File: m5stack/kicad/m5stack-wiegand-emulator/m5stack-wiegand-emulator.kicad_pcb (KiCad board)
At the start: 2 copper layers, 50 x 50 mm, 58 parts, among them J1 2x15 socket header, J2 2x15 pin header, J3 1x5 female, M1 M5 Stack 3.1mm mounting hole, M12 M5 Stack 1.1mm reference hole, M2 M5 Stack 3.1mm mounting hole, M3 M5 Stack 3.1mm mounting hole, M4 M5 Stack 3.1mm mounting hole, M5 M5 Stack 2mm mounting hole, M6 M5 Stack 2mm mounting hole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

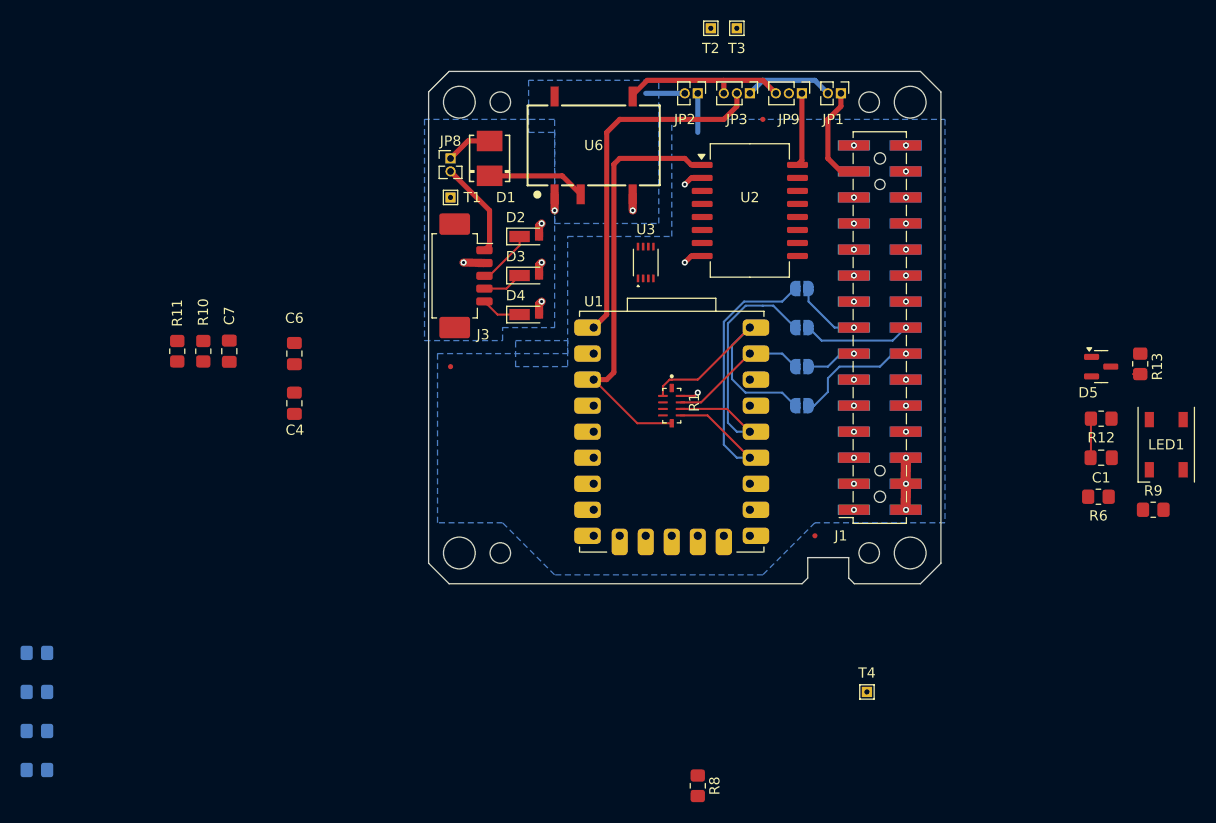
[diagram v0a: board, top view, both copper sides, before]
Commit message: M5: routed DI/DO signals
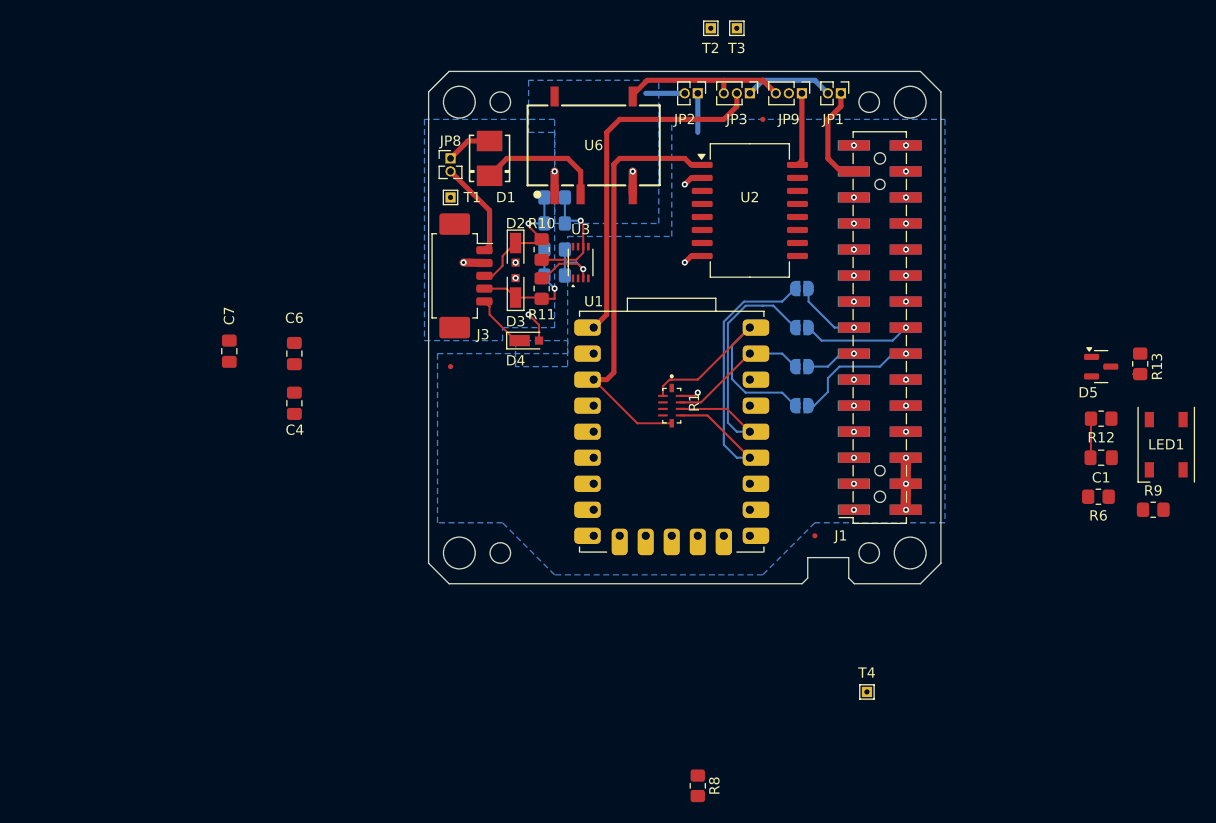
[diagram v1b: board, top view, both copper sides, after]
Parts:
- moved R19 69.9 mm to (101.6, 83.8)
- moved R15 69.9 mm to (101.6, 76.2)
- moved R16 69.0 mm to (101.6, 81.3)
- moved R14 65.6 mm to (101.6, 78.7)
- moved R11 36.1 mm to (100.3, 85.1)
- moved R10 34.5 mm to (100.3, 81.3)
- moved U3 6.35 mm to (104.1, 82.5)
- moved D4 2.54 mm to (99.1, 90.2)
- moved D2 1.98 mm to (97.8, 81.5), turned to -90 degrees
- moved D3 1.80 mm to (97.8, 85.1), turned to 90 degrees
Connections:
- R10 pad 1: Net-(U3-1Y) -> /DI
- R10 pad 2: /DI -> Net-(U3-1Y)
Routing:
- net Net-(U3-1Y): track 0.00 -> 11.8 mm, vias 0 -> 1
- net Net-(U3-2Y): track 0.00 -> 10.4 mm, vias 0 -> 1
- net /DO: track 4.35 -> 12.5 mm, vias 0 -> 1
- net /DI: track 5.93 -> 13.8 mm, vias 0 -> 1
- net Net-(D1-K): track 9.64 -> 12.4 mm
- net /LED: track 3.96 -> 5.47 mm

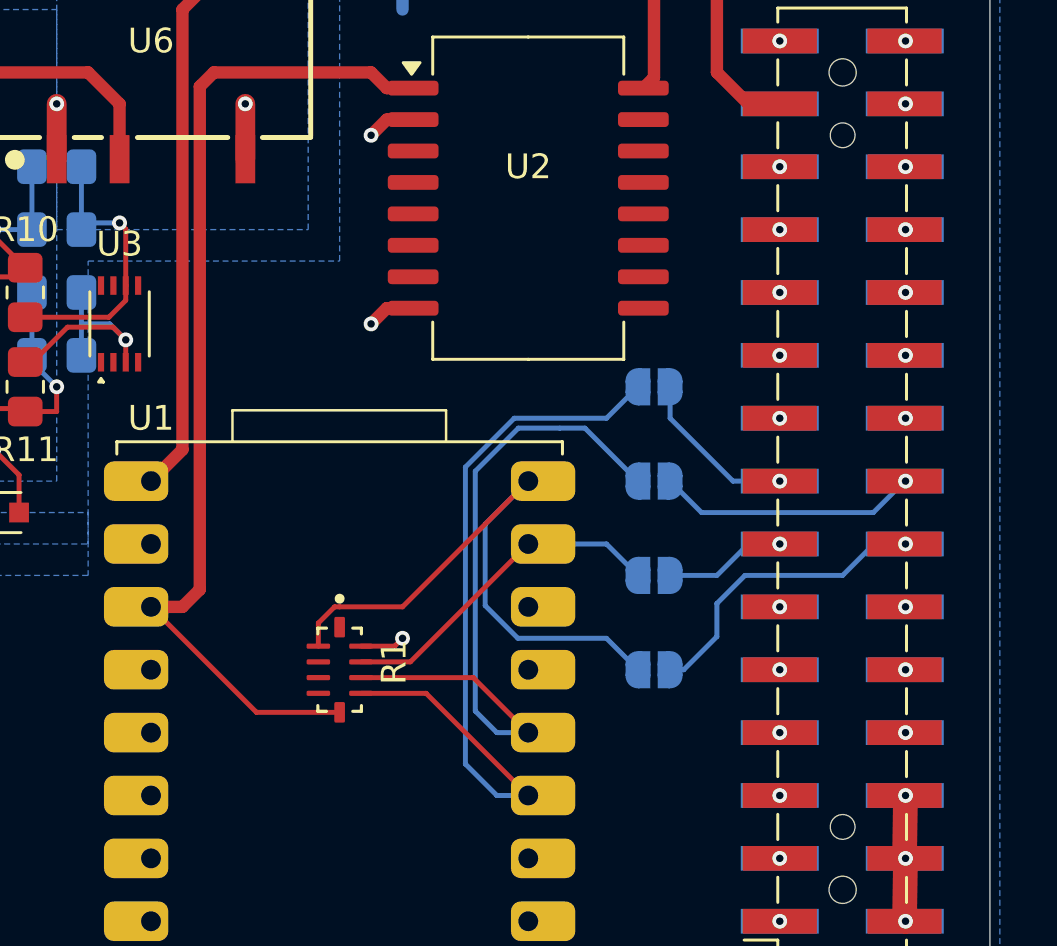
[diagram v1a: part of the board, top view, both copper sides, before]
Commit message: M5: moved DI/DO to GP28/29"
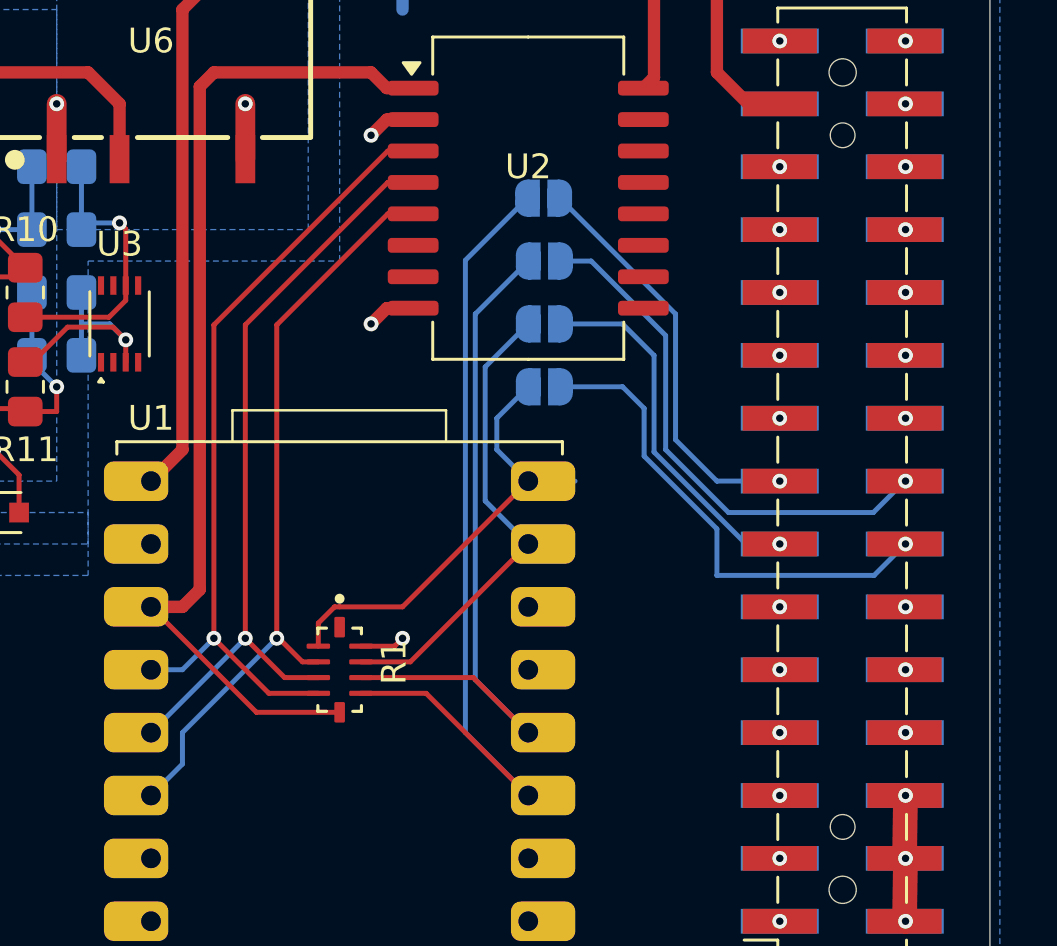
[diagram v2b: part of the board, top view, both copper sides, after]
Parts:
- moved JP4 12.3 mm to (121.3, 85.1)
- moved JP5 11.1 mm to (121.3, 82.5)
- moved JP6 9.93 mm to (121.3, 80.0)
- moved JP7 8.83 mm to (121.3, 77.5)
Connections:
- U1 pad 10: Net-(R1B-R2.2) -> unconnected-(U1-GP13-Pad10)
- U1 pad 4: unconnected-(U1-GP29-Pad4) -> Net-(R1D-R4.2)
- U1 pad 5: unconnected-(U1-GP28-Pad5) -> Net-(R1C-R3.2)
- U1 pad 6: unconnected-(U1-GP27-Pad6) -> Net-(R1B-R2.2)
- U1 pad 8: Net-(R1D-R4.2) -> unconnected-(U1-GP15-Pad8)
- U1 pad 9: Net-(R1C-R3.2) -> unconnected-(U1-GP14-Pad9)
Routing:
- net Net-(R1D-R4.2): track 0.00 -> 31.8 mm, vias 0 -> 1
- net Net-(R1C-R3.2): track 0.00 -> 30.8 mm, vias 0 -> 1
- net Net-(R1B-R2.2): track 0.00 -> 30.6 mm, vias 0 -> 1
- net /TXD1: track 4.96 -> 16.1 mm
- net /RXD2: track 10.5 -> 21.3 mm
- net /TXD2: track 6.75 -> 16.6 mm
- net /RXD1: track 12.4 -> 19.9 mm
- net Net-(JP4-B): track 24.8 -> 18.5 mm
- net Net-(JP5-B): track 13.7 -> 19.1 mm
- net Net-(JP7-B): track 31.8 -> 34.7 mm

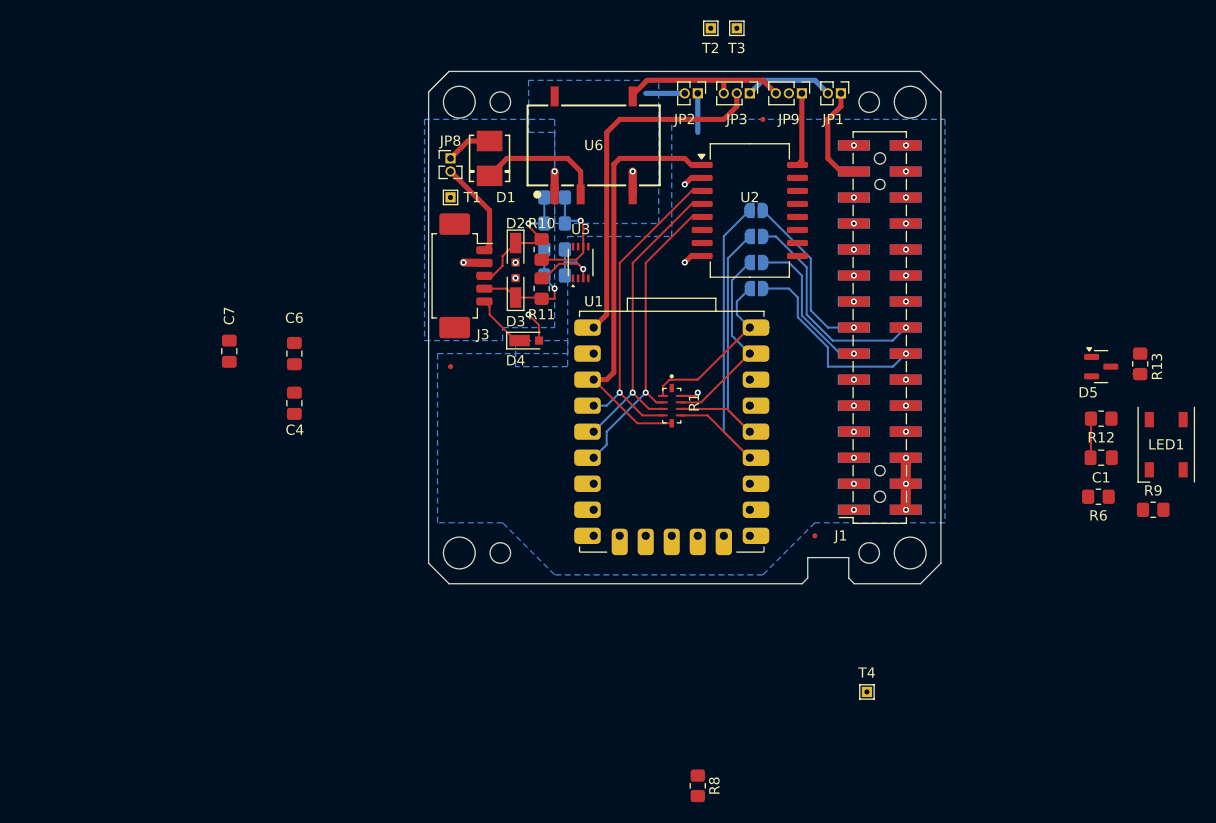
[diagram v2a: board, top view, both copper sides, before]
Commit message: M5: routing LED IN signal
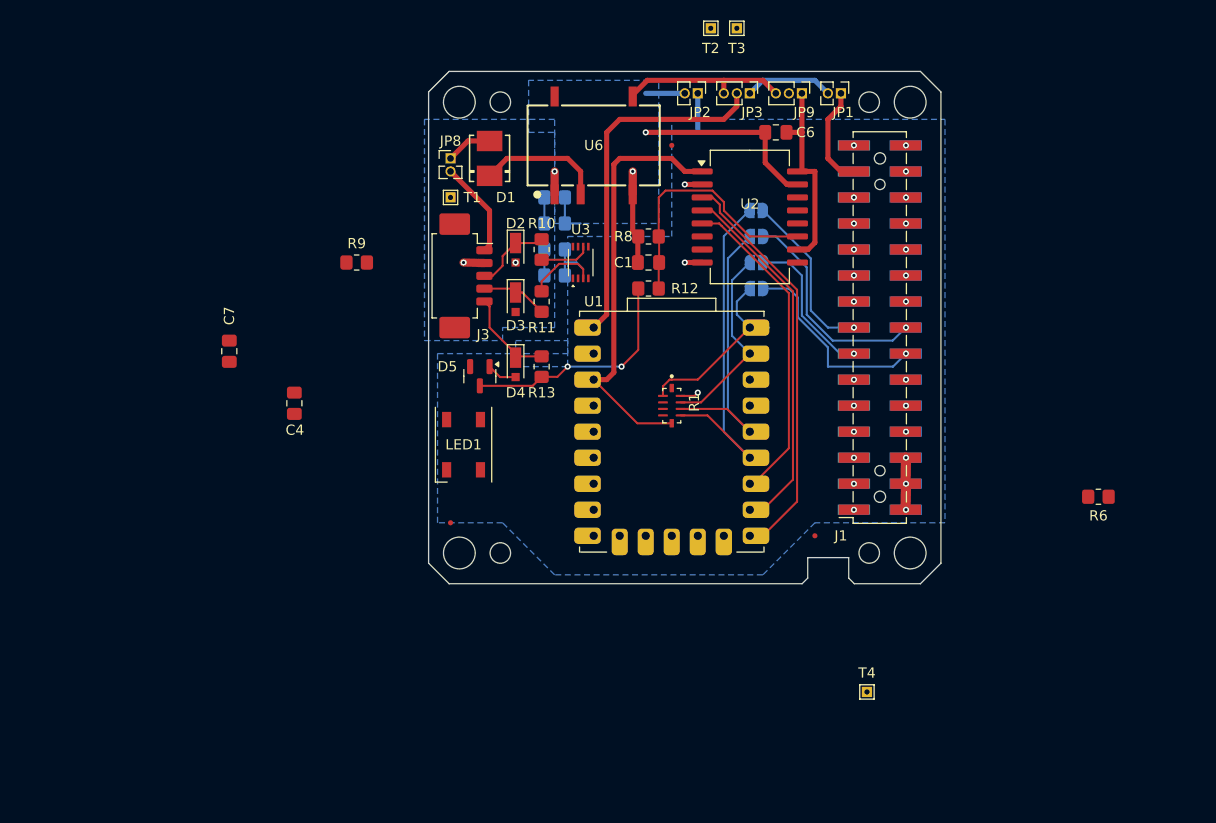
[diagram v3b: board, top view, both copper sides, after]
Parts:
- moved R9 81.4 mm to (82.3, 82.5)
- moved LED1 68.6 mm to (92.7, 100.3)
- moved D5 60.6 mm to (94.3, 93.6), turned to -90 degrees
- moved R13 58.4 mm to (100.3, 92.7)
- moved R8 53.8 mm to (110.8, 80.0), turned to 180 degrees
- moved C6 51.7 mm to (123.2, 69.8), turned to 180 degrees
- moved C1 48.1 mm to (110.8, 82.5), turned to 180 degrees
- moved R12 46.0 mm to (110.8, 85.1), turned to 180 degrees
- moved F3 15.2 mm to (91.4, 108.0)
- moved F2 9.25 mm to (113.0, 71.1)
- moved D4 2.84 mm to (97.8, 92.7), turned to -90 degrees
- moved D3 1.27 mm to (97.8, 86.4), turned to -90 degrees
- moved R11 1.27 mm to (100.3, 86.4)
- moved U2 0.64 mm to (120.7, 78.1)
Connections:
- U1 pad 15: unconnected-(U1-GP8-Pad15) -> Net-(R1D-R4.2)
- U1 pad 16: unconnected-(U1-GP7-Pad16) -> Net-(R1C-R3.2)
- U1 pad 17: unconnected-(U1-GP6-Pad17) -> Net-(R1B-R2.2)
- U1 pad 4: Net-(R1D-R4.2) -> unconnected-(U1-GP29-Pad4)
- U1 pad 5: Net-(R1C-R3.2) -> unconnected-(U1-GP28-Pad5)
- U1 pad 6: Net-(R1B-R2.2) -> unconnected-(U1-GP27-Pad6)
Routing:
- net GND1: track 13.3 -> 39.1 mm, vias 6 -> 5
- net Net-(D5-COM): track 0.79 -> 22.9 mm, vias 0 -> 2
- net Net-(U2-IND): track 3.83 -> 25.1 mm
- net VISO: track 7.16 -> 19.7 mm
- net Net-(R1D-R4.2): track 31.8 -> 40.1 mm, vias 1 -> 0
- net Net-(R1C-R3.2): track 30.8 -> 35.9 mm, vias 1 -> 0
- net /LED: track 5.47 -> 9.33 mm
- net /DI: track 13.8 -> 10.4 mm, vias 1 -> 0
- net /DO: track 12.5 -> 9.33 mm, vias 1 -> 0
- net Net-(U3-1Y): track 11.8 -> 9.02 mm, vias 1 -> 0
- net Net-(R1B-R2.2): track 30.6 -> 31.7 mm, vias 1 -> 0
- net Net-(U3-2Y): track 10.4 -> 11.5 mm, vias 1 -> 0
- net GND: track 17.3 -> 16.8 mm

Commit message: M5: rotated U1 and U2 and rerouted
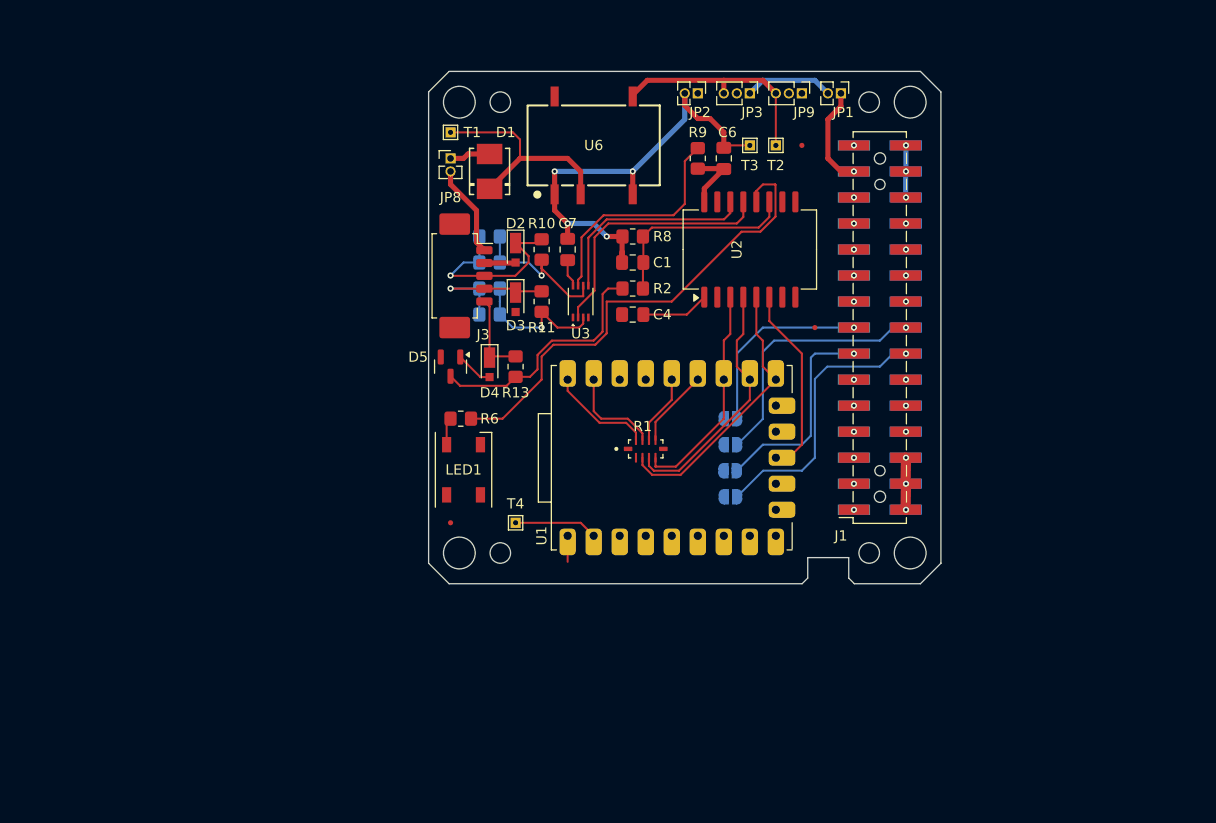
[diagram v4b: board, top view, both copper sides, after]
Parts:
- removed R12: 470, Resistor_SMD:R_0805_2012Metric_Pad1.20x1.40mm_HandSolder
- added R2: 470, Resistor_SMD:R_0805_2012Metric_Pad1.20x1.40mm_HandSolder, F.Cu at (109.2, 85.1)
- moved R6 62.7 mm to (92.4, 97.8), turned to 180 degrees
- moved G*** 42.2 mm to (113.0, 77.5)
- moved T4 38.1 mm to (97.8, 108.0)
- moved R9 34.8 mm to (115.6, 72.4), turned to 90 degrees
- moved C7 34.5 mm to (102.9, 81.3)
- moved C4 34.1 mm to (109.2, 87.6), turned to 180 degrees
- moved JP5 20.5 mm to (118.7, 102.9)
- moved JP4 20.5 mm to (118.8, 105.4)
- moved JP6 20.5 mm to (118.8, 100.3)
- moved JP7 20.5 mm to (118.8, 97.8)
- moved F1 20.3 mm to (127.0, 88.9)
- moved T2 13.1 mm to (123.2, 71.1)
- moved F2 12.7 mm to (125.7, 71.1)
- moved T3 11.5 mm to (120.7, 71.1)
- moved R14 7.41 mm to (95.2, 82.5)
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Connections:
- C7 pad 1: VISO -> Net-(JP9-C)
- R1 pad 10: GND -> Net-(JP4-B)
- R1 pad 2: Net-(JP4-B) -> GND
- U1 pad 15: Net-(R1D-R4.2) -> Net-(R1B-R2.2)
- U1 pad 17: Net-(R1B-R2.2) -> Net-(R1D-R4.2)
- U3 pad 2: Net-(U2-OUTA) -> Net-(U2-OUTB)
- U3 pad 5: Net-(U2-OUTB) -> Net-(U2-OUTA)
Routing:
- net Net-(U2-OUTC): track 0.00 -> 47.3 mm
- net +3V3: track 41.3 -> 6.65 mm
- net +5V: track 34.6 -> 2.54 mm
- net Net-(JP7-B): track 34.7 -> 7.61 mm
- net Net-(U2-OUTB): track 0.00 -> 25.3 mm
- net Net-(U3-1OE): track 0.00 -> 22.3 mm
- net Net-(JP6-B): track 28.5 -> 6.82 mm
- net Net-(U2-OUTA): track 0.00 -> 20.6 mm
- net Net-(U1-GP11): track 0.00 -> 18.8 mm
- net Net-(R1D-R4.2): track 40.1 -> 21.6 mm
- net GND1: track 39.1 -> 53.4 mm, vias 5 -> 4
- net VISO: track 19.7 -> 6.60 mm
- net Net-(R1C-R3.2): track 35.9 -> 24.5 mm
- net Net-(JP5-B): track 19.1 -> 9.39 mm
- net Net-(D1-K): track 12.4 -> 21.8 mm
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- removed copper zone on B.Cu, net GND
- removed copper zone on B.Cu, net GND1
